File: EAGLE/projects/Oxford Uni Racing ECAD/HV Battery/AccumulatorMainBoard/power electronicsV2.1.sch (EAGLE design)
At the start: 103 parts, among them IC1 4043D, IC10 74AHC1G08DBV, IC2 SE555D, IC3 4011D, IC5 4043D, IC6 4011D, IC7 4011D, IC8 4011D, IC9 4011D, K1 T9AS1D12-48=T9A, K2 T9AS5D12-12=T9A, K3 T9AS1D12-48=T9A, K4 T9AS1D12-48=T9A, Q1 BSS138, Q2 BSS138, Q3 BSS138, Q4 BSS138, X1 CAN 1, X2 CAN 2

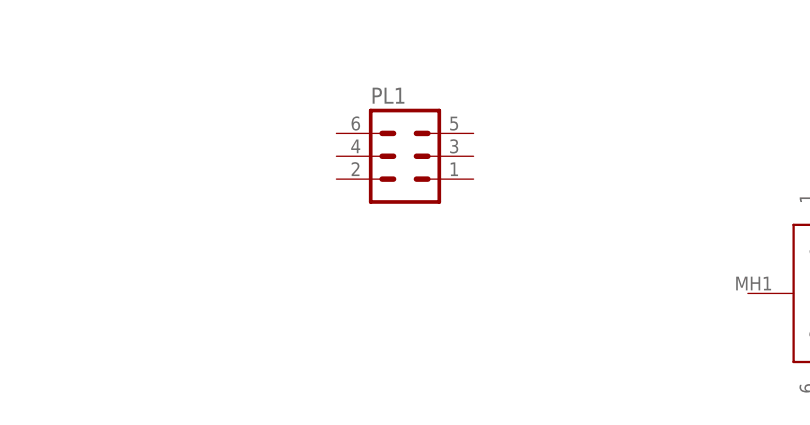
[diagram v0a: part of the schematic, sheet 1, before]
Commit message: precharge board/ main board transfer
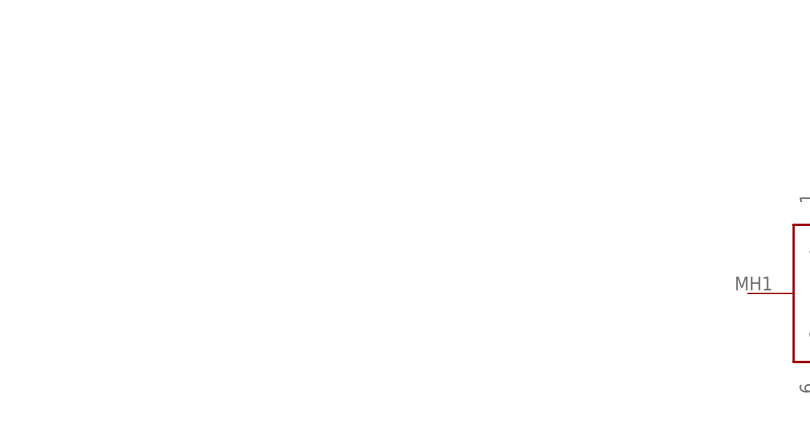
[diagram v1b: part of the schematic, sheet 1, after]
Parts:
- removed PL1: (no value), con-harting-v:06V
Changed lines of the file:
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@@
 <part name="CAN1" library="LD09P24A4GV00LF" deviceset="LD09P24A4GV00LF" device=""/>
 <part name="CAN2" library="LD09P24A4GV00LF" deviceset="LD09P24A4GV00LF" device=""/>
-<part name="PL1" library="con-harting-v" library_urn="urn:adsk.eagle:library:150" deviceset="06V" device="" package3d_urn="urn:adsk.eagle:package:7042/1"/>
 </parts>
 <sheets>
@@
 <attribute name="VALUE" x="184.15" y="149.86" size="1.778" layer="96" align="center-left"/>
 </instance>
-<instance part="PL1" gate="G$1" x="124.46" y="154.94" smashed="yes">
-<attribute name="VALUE" x="120.65" y="147.32" size="1.778" layer="96"/>
-<attribute name="NAME" x="120.65" y="160.782" size="1.778" layer="95"/>
-</instance>
 </instances>

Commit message: Feedback addressed
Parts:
- removed TP28, TP29, TP30, TP31: TPTP17R, testpad:TPTP17R
- removed X1: CAN 1, con-subd:F09V
- removed X2: CAN 2, con-subd:F09V
- added TP11, TP20, TP21, TP22: TPSTP11R, testpad:TPSTP11R
- BMS_I/O, ISOMETER_I/O, MISC_I/O: value T821108A1S100CEU -> T816108A1S102CEU; device SamacSys_Parts:T821108A1S100CEU -> T816108A1S102CEU:T816108A1S102CEU
- TP12, TP13, TP14, TP15, TP16, TP17, TP18, TP19, TP23: value TPTP17R -> TPSTP11R; device testpad:TPTP17R -> testpad:TPSTP11R
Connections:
- net +12V: now also TP11.PP, TP14.PP, TP15.PP, TP22.PP, TP3.PP; no longer R24.1, R25.1, TP14.TP, TP15.TP, TP19.TP, TP28.TP
- net CAN1_H: no longer X1.3
- net CAN1_L: no longer X1.5
- net CAN2_H: no longer X2.3
- net CAN2_L: no longer X2.5
- net DISCHARGE_ENABLE: now also TP18.PP; no longer TP18.TP
- net GND: now also R24.1, R25.1
- net IMD_COIL_OUT: now also TP19.PP; no longer TP30.TP
- net N$1: now also IC10A.O, TP16.PP; no longer TP16.TP
- net N$10: now also TP12.PP; no longer TP12.TP
- net N$14: now also TP13.PP; no longer TP13.TP
- net N$15: now also TP21.PP; no longer TP23.TP
- net N$8: now also TP17.PP; no longer TP17.TP
- net N$9: now also TP20.PP; no longer TP31.TP
- net PRECHARGE_SELECT: now also TP23.PP; no longer TP29.TP
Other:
- moved on the sheet: BMS_I/O, BMS_POWER/GND-1, BMS_POWER/GND-2, BMS_POWER/GND-3, C9, D2, D5, F1, F2, H1, H2, H3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

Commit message: small changes to schematic on acc main board and more feedback
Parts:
- removed TP3: TPSTP11R, testpad:TPSTP11R
- added TP24: TPSTP11R, testpad:TPSTP11R
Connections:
- net +12V: no longer C9.2, IC1A.R2, IC1A.R3, IC1A.S2, IC1A.S3, K1.COM, K4.NO, OK2.GND, PRECHARGE/AIRS-3.S, PRECHARGE/AIRS-4.S, PRECHARGE/AIRS-6.S, Q1.S, Q2.S, Q4.S, R13.1, R19.1, R3.2, TP11.PP, TP14.PP, TP3.PP
- net GND: now also C9.2, IC1A.R2, IC1A.R3, IC1A.S2, IC1A.S3, K1.COM, K4.NO, OK2.GND, PRECHARGE/AIRS-3.S, PRECHARGE/AIRS-4.S, PRECHARGE/AIRS-6.S, Q1.S, Q2.S, Q4.S, R13.1, R19.1, R3.2, TP11.PP, TP14.PP, TP24.PP
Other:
- moved on the sheet: D7, D8, EMSDC-1, K1, K4, Q1, TP14, TP15, TP18, TP19, TP21, TP7

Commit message: most of the feedback addressed
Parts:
- removed IC10: 74AHC1G08DBV, 74xx-little-us:74AHC1G08DBV
- added LED7, LED8: (no value), led:LEDSML0805
- added R12, R14, R15: (no value), rcl:R-EU_R0805
- TP1, TP10, TP11, TP12, TP13, TP14, TP15, TP16, TP17, TP18, TP19, TP2, TP20, TP21, TP22, TP23, TP24, TP4, TP5, TP6, TP7: value TPSTP11R -> TPPAD1-17; device testpad:TPSTP11R -> testpad:TPPAD1-17
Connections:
- new net N$18: LED7.A, R14.1
- new net N$20: LED8.A, R15.1
- new net N$6: IC9C.I0, IC9C.I1, IC9D.O
- net +12V: now also R14.2, R15.2, TP15.TP, TP22.TP; no longer TP15.PP, TP22.PP
- net CHARGE_SAFE: now also IC9D.I0; no longer IC10A.I0
- net DISCHARGE_ENABLE: now also R12.2, TP18.TP, TP7.TP; no longer TP18.PP, TP7.PP
- net GND: now also R12.1, TP11.TP, TP14.TP, TP24.TP; no longer IC9C.I0, IC9C.I1, IC9D.I0, IC9D.I1, TP11.PP, TP14.PP, TP24.PP
- net IMD_COIL_OUT: now also LED8.C, TP19.TP; no longer TP19.PP
- net N$1: now also IC9C.O, TP16.TP; no longer IC10A.O, TP16.PP
- net N$10: now also TP12.TP, TP2.TP; no longer TP12.PP, TP2.PP
- net N$13: now also IC9D.I1; no longer IC10A.I1
- net N$14: now also TP13.TP; no longer TP13.PP
- net N$15: now also LED7.C, TP21.TP; no longer TP21.PP
- net N$5: now also TP1.TP; no longer TP1.PP
- net N$8: now also TP17.TP, TP6.TP; no longer TP17.PP, TP6.PP
- net N$9: now also TP20.TP, TP5.TP; no longer TP20.PP, TP5.PP
- net OK_HS: now also TP10.TP; no longer TP10.PP
- net PRECHARGE_SELECT: now also TP23.TP; no longer TP23.PP
- net STARTUP_RESET: now also TP4.TP; no longer TP4.PP
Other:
- moved on the sheet: C9, D1, EMSDC-5, IC1, IC9C, IC9D, K1, K2, LED1, LED4, LED5, PRECHARGE/AIRS-1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

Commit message: most of the feedback addressed ctd
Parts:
- removed R17: (no value), rcl:R-EU_R0805
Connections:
- removed net N$13: IC9D.I1, LED4.C
- net DISCHARGE_ENABLE: now also IC9D.I1, LED4.C
- net GND: no longer R17.1
- net N$8: no longer R17.2
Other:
- moved on the sheet: D1, EMSDC-5, K2, LED1, PRECHARGE/AIRS-1, PRECHARGE/AIRS-2, PRECHARGE/AIRS-5, R20, TP22, TP23

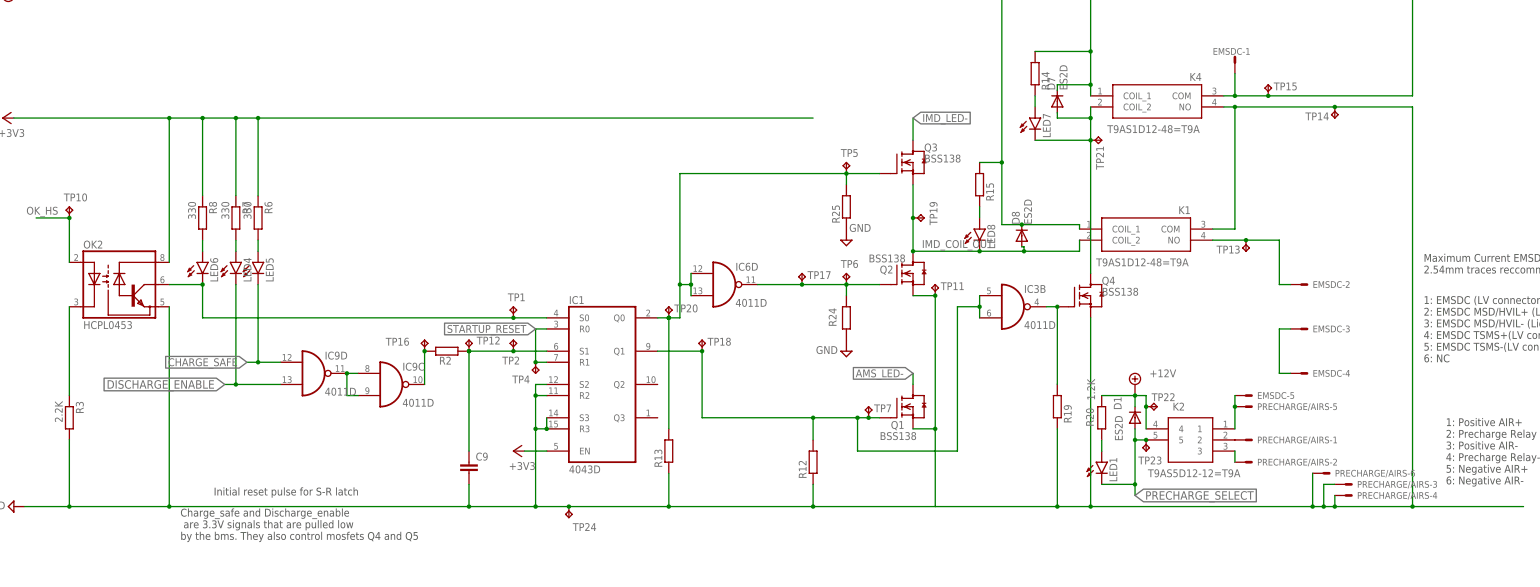
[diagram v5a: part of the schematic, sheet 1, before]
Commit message: Minor changes to layout added values to RC circuit
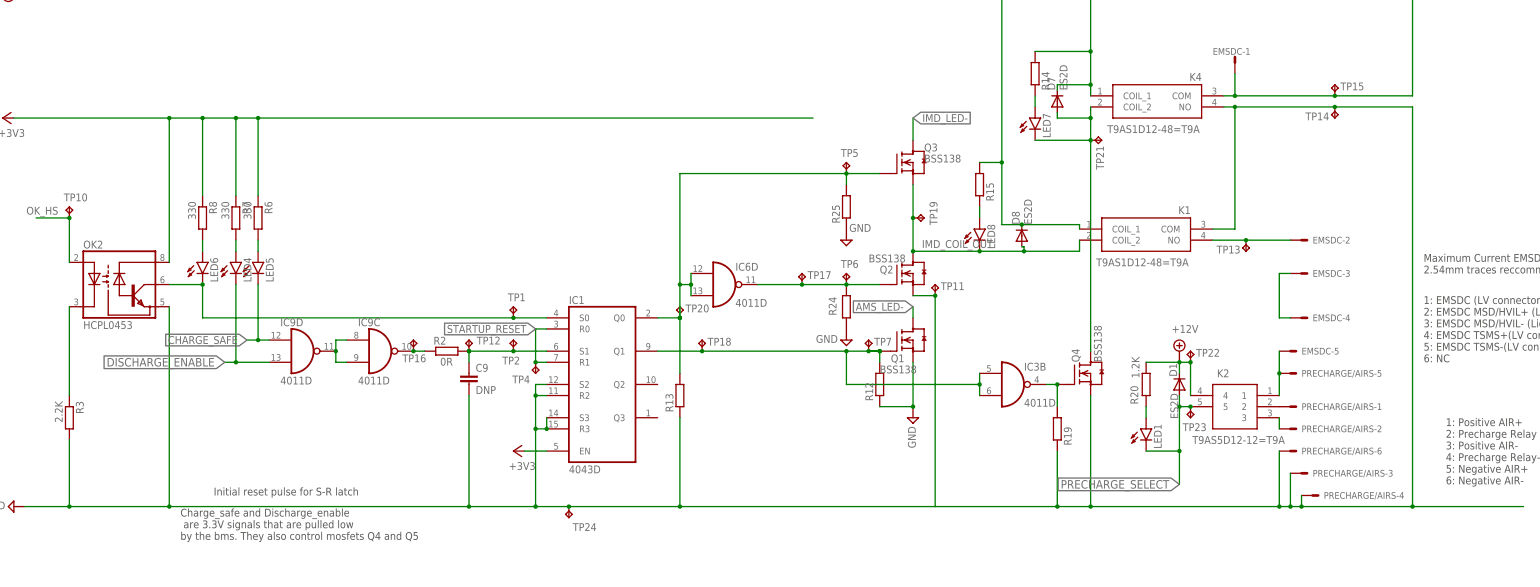
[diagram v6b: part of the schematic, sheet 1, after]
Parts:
- C9: value (none) -> DNP
- R2: value (none) -> 0R
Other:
- moved on the sheet: C9, D1, EMSDC-2, EMSDC-3, EMSDC-4, EMSDC-5, IC3B, IC9C, IC9D, K2, LED1, PRECHARGE/AIRS-1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

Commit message: Feedback
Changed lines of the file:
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@@
 <part name="FRAME3" library="frames" library_urn="urn:adsk.eagle:library:229" deviceset="A3L-LOC" device=""/>
 <part name="IC9" library="40xx" library_urn="urn:adsk.eagle:library:80" deviceset="4011" device="D" package3d_urn="urn:adsk.eagle:package:823/2"/>
-<part name="SUPPLY12" library="supply2" library_urn="urn:adsk.eagle:library:372" deviceset="GND" device=""/>
 <part name="H1" library="holes" library_urn="urn:adsk.eagle:library:237" deviceset="MOUNT-HOLE" device="3.2" package3d_urn="urn:adsk.eagle:package:14275/1"/>
 <part name="H2" library="holes" library_urn="urn:adsk.eagle:library:237" deviceset="MOUNT-HOLE" device="3.2" package3d_urn="urn:adsk.eagle:package:14275/1"/>
@@
 <attribute name="VALUE" x="-10.16" y="30.48" size="1.778" layer="96"/>
 </instance>
-<instance part="SUPPLY12" gate="GND" x="134.62" y="-50.8" smashed="yes" rot="R270">
-<attribute name="VALUE" x="127.635" y="-51.435" size="1.778" layer="96"/>
-</instance>
 <instance part="R24" gate="G$1" x="119.38" y="48.26" smashed="yes" rot="R90">
 <attribute name="NAME" x="117.1194" y="46.228" size="1.778" layer="95" rot="R90"/>
@@
 </segment>
 <segment>
-<wire x1="137.16" y1="-50.8" x2="165.1" y2="-50.8" width="0.1524" layer="91"/>
-<pinref part="SUPPLY12" gate="GND" pin="GND"/>
-</segment>
-<segment>

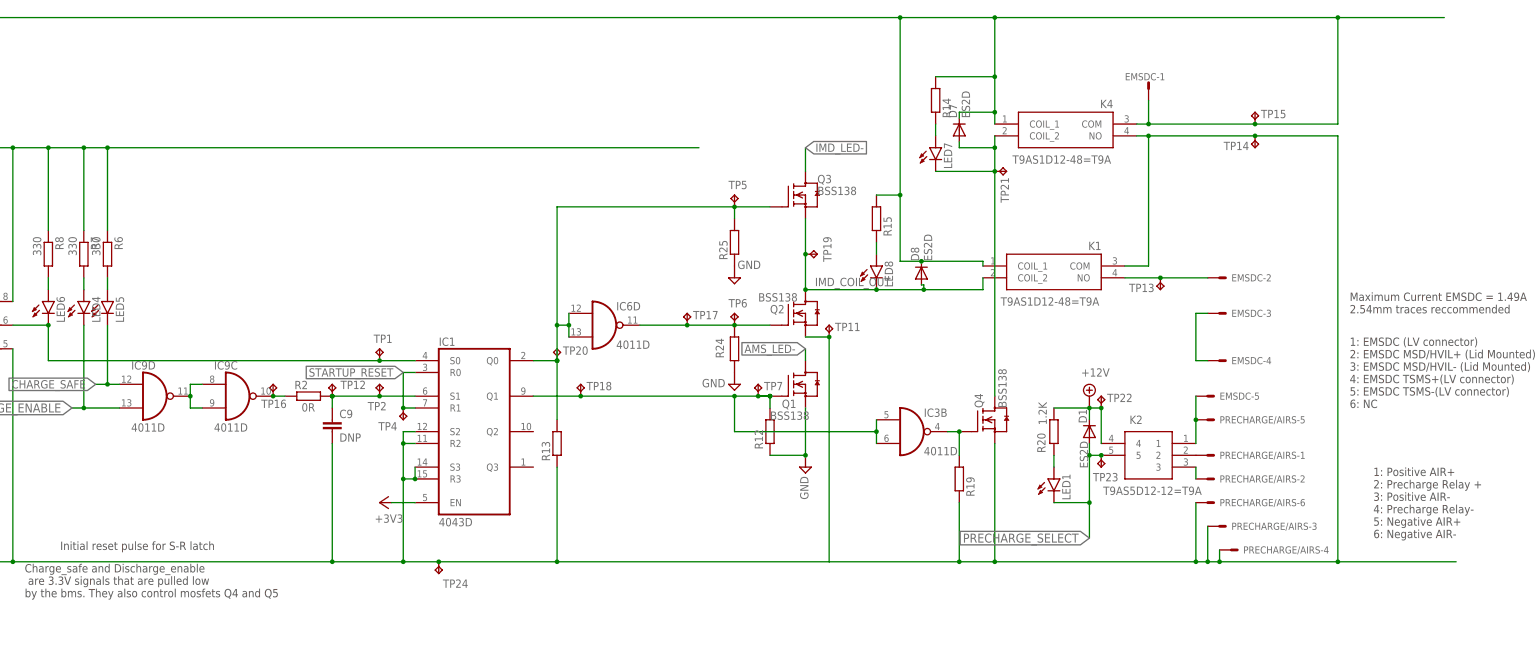
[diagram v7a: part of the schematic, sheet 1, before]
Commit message: Removed some testpoints and added a few. Also fixed EMSDC relay path
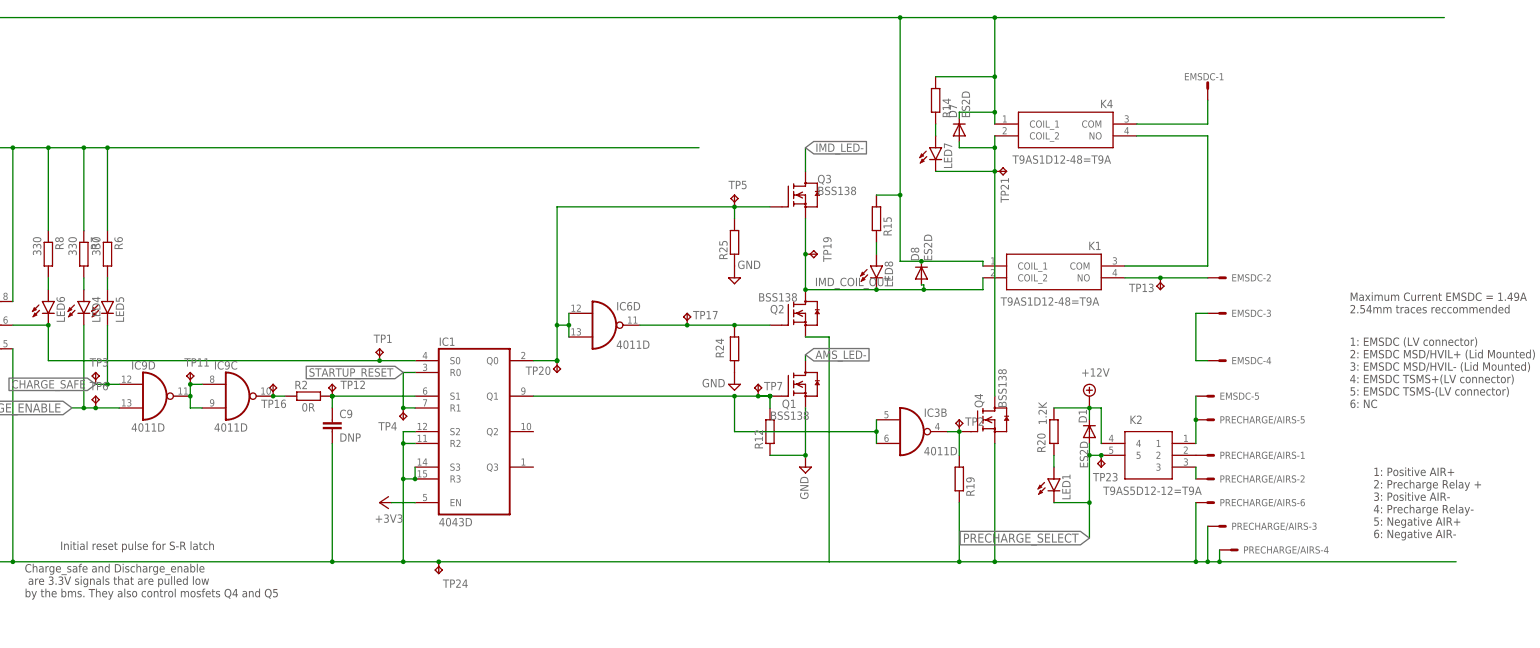
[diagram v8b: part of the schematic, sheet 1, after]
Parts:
- removed R13: (no value), rcl:R-EU_R0805
- removed TP14, TP15, TP18, TP22: TPPAD1-17, testpad:TPPAD1-17
- added TP3: TPPAD1-17, testpad:TPPAD1-17
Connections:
- new net N$13: EMSDC-1.S, K4.COM
- new net N$21: K1.COM, K4.NO
- net +12V: no longer EMSDC-1.S, K4.COM, TP15.TP, TP22.TP
- net CHARGE_SAFE: now also TP3.TP
- net DISCHARGE_ENABLE: now also TP6.TP; no longer TP18.TP
- net GND: no longer K1.COM, K4.NO, R13.1, TP11.TP, TP14.TP
- net N$10: no longer TP2.TP
- net N$16: now also TP2.TP
- net N$6: now also TP11.TP
- net N$8: no longer TP6.TP
- net N$9: no longer R13.2
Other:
- moved on the sheet: EMSDC-1, TP11, TP2, TP20, TP6
